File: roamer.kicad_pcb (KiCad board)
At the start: 2 copper layers, 0 parts

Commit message: Fixing footprint imports
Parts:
- added C1: 10uF, Inductor_SMD:L_0805_2012Metric, F.Cu at (194.5, 139.5)
- added C10: 10uF, Inductor_SMD:L_0805_2012Metric, F.Cu at (233.5, 128.4)
- added C11: 1uF, Capacitor_SMD:C_0603_1608Metric, F.Cu at (237.8, 122.5)
- added C12: 1uF, Capacitor_SMD:C_0603_1608Metric, F.Cu at (233.2, 100.8)
- added C13: 10uF, Inductor_SMD:L_0805_2012Metric, F.Cu at (226.7, 115.4)
- added C14: 1uF, Capacitor_SMD:C_0603_1608Metric, F.Cu at (226.8, 96.2)
- added C15: 1uF, Capacitor_SMD:C_0603_1608Metric, F.Cu at (226.8, 98.7)
- added C2: 22pF, Capacitor_SMD:C_0603_1608Metric, F.Cu at (198.7, 150.8)
- added C3: 10uF, Inductor_SMD:L_0805_2012Metric, F.Cu at (217.9, 150.5)
- added C4: 22pF, Capacitor_SMD:C_0603_1608Metric, F.Cu at (198.7, 153.3)
- added C5: 10uF, Inductor_SMD:L_0805_2012Metric, F.Cu at (233.5, 120.2)
- added C6: 10uF, Inductor_SMD:L_0805_2012Metric, F.Cu at (233.5, 122.9)
- added C7: 1uF, Capacitor_SMD:C_0603_1608Metric, F.Cu at (237.8, 120.0)
- added C8: 10uF, Inductor_SMD:L_0805_2012Metric, F.Cu at (233.5, 125.7)
- added C9: 10uF, Inductor_SMD:L_0805_2012Metric, F.Cu at (194.5, 113.9)
- added CHG1: ORANGE, LED_SMD:LED_0805_2012Metric, F.Cu at (222.4, 150.7)
- added D1: WS2812B3535, LED_SMD:LED_SK6812MINI_PLCC4_3.5x3.5mm_P1.75mm, F.Cu at (241.2, 151.1)
- added D4: MBR120, Diode_SMD:D_SOD-123, F.Cu at (242.9, 132.6)
- added J1: Conn_Coaxial_Small, Connector_Coaxial:U.FL_Molex_MCRF_73412-0110_Vertical, F.Cu at (189.2, 141.2)
- added J2: S2B-PH-K-SLFSN, footprints:CONN_S2B-PH-K-S_JST, F.Cu at (215.5, 142.1)
- added J3: Conn_02x05_Odd_Even, Connector_PinHeader_1.27mm:PinHeader_2x05_P1.27mm_Vertical_SMD, F.Cu at (236.0, 110.8)
- added J4: Conn_Coaxial_Small, Connector_Coaxial:U.FL_Molex_MCRF_73412-0110_Vertical, F.Cu at (189.2, 115.6)
- added J8: MEM2075-00-140-01-A, footprints:GCT_MEM2075-00-140-01-A, F.Cu at (219.4, 132.0)
- added JP1: SolderJumper_2_Open, Jumper:SolderJumper-2_P1.3mm_Open_TrianglePad1.0x1.5mm, F.Cu at (227.0, 106.7)
- added L1: RED, LED_SMD:LED_0805_2012Metric, F.Cu at (221.7, 114.5)
- added L2: 10uH, Inductor_SMD:L_1008_2520Metric, F.Cu at (222.0, 111.2)
- added MCU1: ATSAMD51J19A-A, Package_QFP:TQFP-64_10x10mm_P0.5mm, F.Cu at (217.6, 102.1)
- added Q3: DMP2070UQ-7, Package_TO_SOT_SMD:SOT-23-5_HandSoldering, F.Cu at (242.7, 121.2)
- added R1: 10K, Resistor_SMD:R_0603_1608Metric, F.Cu at (233.2, 103.3)
- added R2: 1K, Capacitor_SMD:C_0603_1608Metric, F.Cu at (222.2, 140.3)
- added R3: 10K, Resistor_SMD:R_0603_1608Metric, F.Cu at (237.8, 125.1)
- added R4: 10K, Resistor_SMD:R_0603_1608Metric, F.Cu at (222.2, 142.8)
- added R6: 10K, Resistor_SMD:R_0603_1608Metric, F.Cu at (226.8, 101.2)
- added R7: 2.2K, Resistor_SMD:R_0603_1608Metric, F.Cu at (226.8, 103.7)
- added R9A1: 100K, Resistor_SMD:R_Array_Convex_4x1206, F.Cu at (216.8, 112.7)
- added R9B1: 100K, Resistor_SMD:R_Array_Convex_4x0603, F.Cu at (226.5, 111.7)
- added R9C1: 100K, Resistor_SMD:R_Array_Convex_4x0603, F.Cu at (237.9, 128.7)
- added R9D1: 100K, Resistor_SMD:R_Array_Convex_4x1206, F.Cu at (242.6, 98.3)
- added SW1: KMR2, Button_Switch_SMD:SW_Push_1P1T_NO_CK_KMR2, F.Cu at (234.5, 97.3)
- added TP1: TestPoint, TestPoint:TestPoint_Pad_D1.5mm, F.Cu at (212.2, 111.1)
- added TP2: TestPoint, TestPoint:TestPoint_Pad_D1.5mm, F.Cu at (212.2, 114.6)
- added TP3: TestPoint, TestPoint:TestPoint_Pad_D1.0mm, F.Cu at (238.1, 140.5)
- added TP4: TestPoint, TestPoint:TestPoint_Pad_D1.0mm, F.Cu at (238.1, 143.6)
- added U1: 2MB Flash, Package_SO:SOIC-8_3.9x4.9mm_P1.27mm, F.Cu at (190.4, 149.6)
- added U2: AP2112K-3.3, Package_TO_SOT_SMD:SOT-23-5, F.Cu at (242.5, 128.7)
- added U3: MCP73831-2-OT, Package_TO_SOT_SMD:SOT-23-5, F.Cu at (213.0, 151.5)
- added U4: RFM95W-915S2, RF_Module:HOPERF_RFM9XW_SMD, F.Cu at (196.0, 129.4)
- added U5: RFM69W, RF_Module:HOPERF_RFM69HW, F.Cu at (197.3, 103.8)
- added U7: BME688, Package_LGA:Bosch_LGA-8_3x3mm_P0.8mm_ClockwisePinNumbering, F.Cu at (206.2, 148.7)
- added U8: INA260, Package_SO:TSSOP-16_4.4x5mm_P0.65mm, F.Cu at (231.4, 151.9)
- added X2: 32.768 kHz, Crystal:Crystal_SMD_3215-2Pin_3.2x1.5mm, F.Cu at (199.2, 147.9)
- added X3: microUSB 2.0 B, Connector_USB:USB_Micro-B_Amphenol_10118194_Horizontal, F.Cu at (231.6, 142.1)

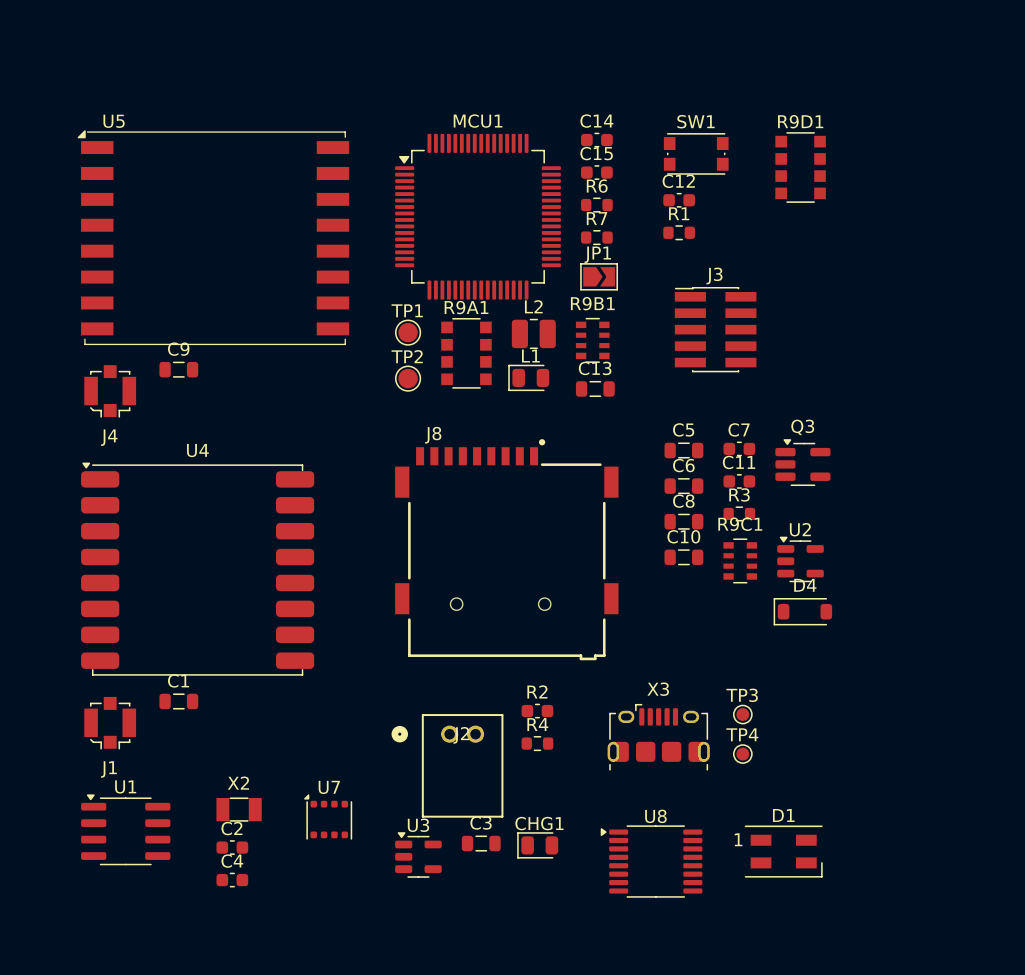
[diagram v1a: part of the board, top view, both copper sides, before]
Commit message: Spamming 0 ohm resistors
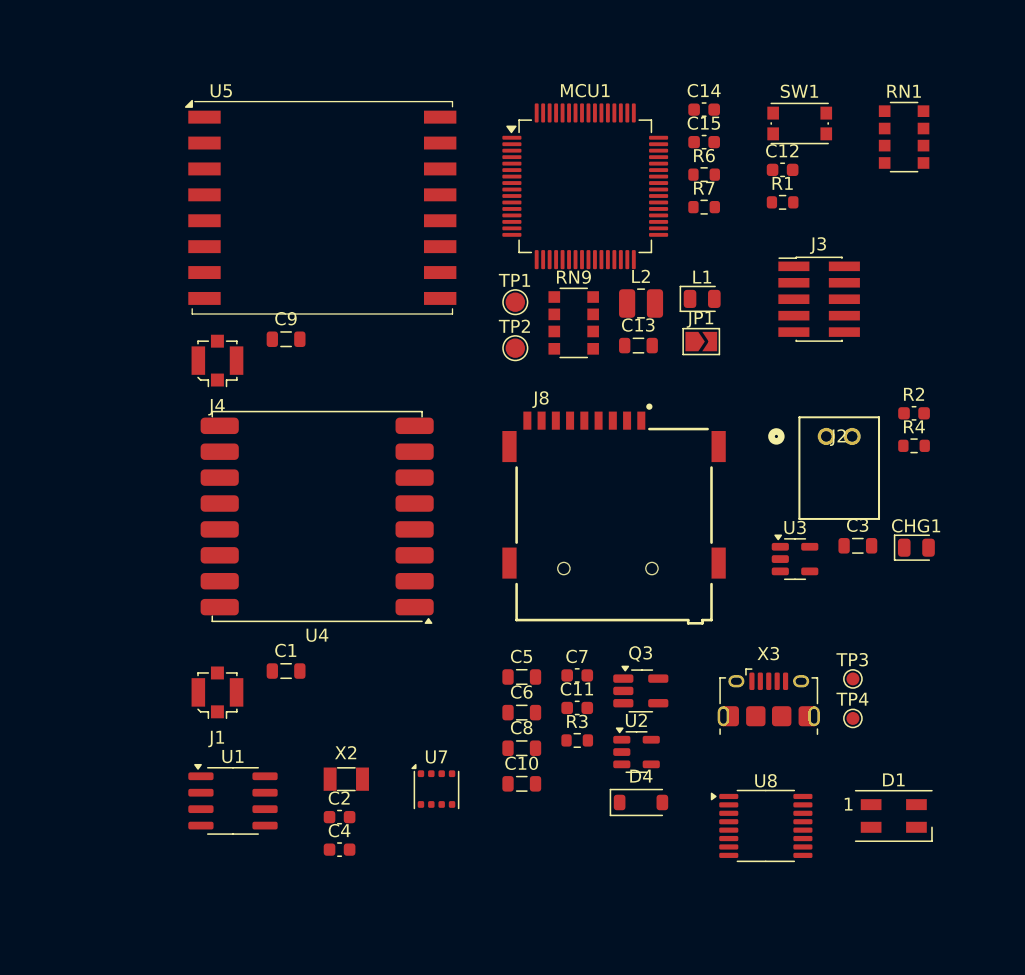
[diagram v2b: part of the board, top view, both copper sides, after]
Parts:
- removed R9A1, R9D1: 100K, Resistor_SMD:R_Array_Convex_4x1206
- removed R9B1, R9C1: 100K, Resistor_SMD:R_Array_Convex_4x0603
- added RN1: 100K, Resistor_SMD:R_Array_Convex_4x1206, F.Cu at (250.5, 96.0)
- added RN9: 100K, Resistor_SMD:R_Array_Convex_4x1206, F.Cu at (225.0, 110.3)
- moved CHG1 37.1 mm to (251.5, 127.7)
- moved U3 37.1 mm to (242.1, 128.5)
- moved J2 37.1 mm to (244.5, 119.1)
- moved R2 37.1 mm to (251.3, 117.3)
- moved C3 37.1 mm to (247.0, 127.5)
- moved R4 37.1 mm to (251.3, 119.8)
- moved Q3 21.5 mm to (230.2, 138.7)
- moved C10 21.5 mm to (221.0, 145.9)
- moved C5 21.5 mm to (221.0, 137.6)
- moved C6 21.5 mm to (221.0, 140.4)
- moved C7 21.5 mm to (225.3, 137.5)
- moved C8 21.5 mm to (221.0, 143.1)
- moved C11 21.5 mm to (225.3, 140.0)
- moved R3 21.5 mm to (225.3, 142.5)
- moved D4 19.4 mm to (230.2, 147.3)
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
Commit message: Starting layout
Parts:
- removed RN1, RN9: 100K, Resistor_SMD:R_Array_Convex_4x1206
- added D2: 1N4148, Diode_SMD:D_SOD-323F, F.Cu at (208.9, 230.5)
- added D3: 1N4148, Diode_SMD:D_SOD-323F, F.Cu at (208.9, 233.4)
- added JP2: SolderJumper_2_Open, Jumper:SolderJumper-2_P1.3mm_Open_TrianglePad1.0x1.5mm, F.Cu at (289.2, 135.2)
- added JP3: SolderJumper_2_Open, Jumper:SolderJumper-2_P1.3mm_Open_TrianglePad1.0x1.5mm, F.Cu at (230.3, 221.5)
- added R10: 0, Resistor_SMD:R_0603_1608Metric, F.Cu at (146.3, 82.2)
- added R11: 0, Resistor_SMD:R_0603_1608Metric, F.Cu at (146.3, 84.8)
- added R12: 0, Resistor_SMD:R_0603_1608Metric, F.Cu at (118.1, 79.7)
- added R13: 0, Resistor_SMD:R_0603_1608Metric, F.Cu at (118.1, 82.2)
- added R14: 0, Resistor_SMD:R_0603_1608Metric, F.Cu at (118.1, 84.8)
- added R15: 0, Resistor_SMD:R_0603_1608Metric, F.Cu at (118.1, 87.3)
- added R16: 0, Resistor_SMD:R_0603_1608Metric, F.Cu at (276.4, 149.3)
- added R17: 0, Resistor_SMD:R_0603_1608Metric, F.Cu at (276.4, 151.8)
- added R18: 0, Resistor_SMD:R_0603_1608Metric, F.Cu at (276.4, 154.4)
- added R19: 0, Resistor_SMD:R_0603_1608Metric, F.Cu at (276.4, 156.9)
- added R20: 10K, Resistor_SMD:R_0603_1608Metric, F.Cu at (146.3, 87.3)
- added R21: 0, Resistor_SMD:R_0603_1608Metric, F.Cu at (276.4, 159.4)
- added R22: 0, Resistor_SMD:R_0603_1608Metric, F.Cu at (146.3, 89.8)
- added R23: 10K, Resistor_SMD:R_0603_1608Metric, F.Cu at (194.3, 80.0)
- added R24: 0, Resistor_SMD:R_0603_1608Metric, F.Cu at (285.0, 130.0)
- added R25: 0, Resistor_SMD:R_0603_1608Metric, F.Cu at (285.0, 132.5)
- added R26: 0, Resistor_SMD:R_0603_1608Metric, F.Cu at (285.0, 135.0)
- added R27: 0, Resistor_SMD:R_0603_1608Metric, F.Cu at (200.1, 224.3)
- added R28: 0, Resistor_SMD:R_0603_1608Metric, F.Cu at (200.1, 226.8)
- added R29: 10K, Resistor_SMD:R_0603_1608Metric, F.Cu at (285.0, 137.5)
- added R30: 10K, Resistor_SMD:R_0603_1608Metric, F.Cu at (296.2, 149.3)
- added R31: 10K, Resistor_SMD:R_0603_1608Metric, F.Cu at (296.2, 151.8)
- added R32: 10K, Resistor_SMD:R_0603_1608Metric, F.Cu at (200.1, 229.3)
- added R33: 0, Resistor_SMD:R_0603_1608Metric, F.Cu at (146.3, 92.3)
- added R34: 10K, Resistor_SMD:R_0603_1608Metric, F.Cu at (194.3, 82.5)
- added R35: 0, Resistor_SMD:R_0603_1608Metric, F.Cu at (146.3, 94.8)
- added R36: 10K, Resistor_SMD:R_0603_1608Metric, F.Cu at (118.1, 89.8)
- added R37: 0, Resistor_SMD:R_0603_1608Metric, F.Cu at (146.3, 97.3)
- added R39: 0, Resistor_SMD:R_0603_1608Metric, F.Cu at (118.1, 92.3)
- added R41: 0, Resistor_SMD:R_0603_1608Metric, F.Cu at (200.1, 231.8)
- added R42: 0, Resistor_SMD:R_0603_1608Metric, F.Cu at (200.1, 234.3)
- added R43: 0, Resistor_SMD:R_0603_1608Metric, F.Cu at (200.1, 236.8)
- added R44: 10K, Resistor_SMD:R_0603_1608Metric, F.Cu at (118.1, 94.8)
- added R45: 0, Resistor_SMD:R_0603_1608Metric, F.Cu at (118.1, 97.3)
- added R5: 10K, Resistor_SMD:R_0603_1608Metric, F.Cu at (200.1, 221.8)
- added R8: 10K, Resistor_SMD:R_0603_1608Metric, F.Cu at (146.3, 79.7)
- added R9: 100K, Resistor_SMD:R_Array_Convex_4x1206, F.Cu at (212.2, 109.2)
- added TP10: TestPoint, TestPoint:TestPoint_Loop_D2.50mm_Drill1.0mm, F.Cu at (204.4, 231.3)
- added TP11: TestPoint, TestPoint:TestPoint_Loop_D2.50mm_Drill1.0mm, F.Cu at (204.4, 236.0)
- added TP12: TestPoint, TestPoint:TestPoint_Loop_D2.50mm_Drill1.0mm, F.Cu at (122.4, 98.4)
- added TP13: TestPoint, TestPoint:TestPoint_Loop_D2.50mm_Drill1.0mm, F.Cu at (122.4, 103.1)
- added TP14: TestPoint, TestPoint:TestPoint_Loop_D2.50mm_Drill1.0mm, F.Cu at (150.7, 98.4)
- added TP15: TestPoint, TestPoint:TestPoint_Loop_D2.50mm_Drill1.0mm, F.Cu at (150.7, 103.0)
- added TP16: TestPoint, TestPoint:TestPoint_Loop_D2.50mm_Drill1.0mm, F.Cu at (291.8, 155.1)
- added TP17: TestPoint, TestPoint:TestPoint_Loop_D2.50mm_Drill1.0mm, F.Cu at (191.7, 230.7)
- added TP18: TestPoint, TestPoint:TestPoint_Loop_D2.50mm_Drill1.0mm, F.Cu at (191.7, 235.3)
- added TP5: TestPoint, TestPoint:TestPoint_Loop_D2.50mm_Drill1.0mm, F.Cu at (191.7, 226.0)
- added TP6: TestPoint, TestPoint:TestPoint_Loop_D2.50mm_Drill1.0mm, F.Cu at (291.8, 150.4)
- added TP7: TestPoint, TestPoint:TestPoint_Loop_D2.50mm_Drill1.0mm, F.Cu at (220.8, 226.7)
- added TP8: TestPoint, TestPoint:TestPoint_Loop_D2.50mm_Drill1.0mm, F.Cu at (280.7, 157.0)
- added TP9: TestPoint, TestPoint:TestPoint_Loop_D2.50mm_Drill1.0mm, F.Cu at (280.7, 161.7)
- moved CHG1 126.4 mm to (185.2, 235.3)
- moved R2 126.4 mm to (185.0, 224.9)
- moved U3 126.4 mm to (175.8, 236.2)
- moved C3 126.4 mm to (180.7, 235.2)
- moved R4 126.4 mm to (185.0, 227.4)
- moved C12 122.5 mm to (236.5, 220.9)
- moved R1 122.5 mm to (236.5, 223.4)
- moved SW1 118.9 mm to (244.7, 213.8)
- moved L1 107.7 mm to (208.8, 213.0)
- moved C13 107.7 mm to (203.9, 216.6)
- moved JP1 107.7 mm to (208.8, 216.2)
- moved L2 107.7 mm to (204.1, 213.3)
- moved TP1 106.5 mm to (199.8, 213.2)
- moved TP2 106.5 mm to (199.8, 216.8)
- moved C2 87.9 mm to (236.5, 231.2)
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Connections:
- net +3.3V renamed Net-(U7-VDD)
- net /Power - Battery/STAT renamed Net-(U3-STAT)
- C1 pad 2: +3V3 -> Net-(U4-3.3V)
- C9 pad 2: +3V3 -> Net-(U5-3.3V)
- J3 pad 1: unconnected-(J3-Pin_1-Pad1) -> Net-(J3-Pin_1)
- J3 pad 10: /MCU/I2C.SDA -> Net-(D3-K)
- J3 pad 2: unconnected-(J3-Pin_2-Pad2) -> Net-(J3-Pin_1)
- J3 pad 3: unconnected-(J3-Pin_3-Pad3) -> GND
- J3 pad 4: unconnected-(J3-Pin_4-Pad4) -> GND
- J3 pad 5: unconnected-(J3-Pin_5-Pad5) -> Net-(D2-K)
- J3 pad 7: unconnected-(J3-Pin_7-Pad7) -> Net-(J3-Pin_7)
- J3 pad 8: /MCU/I2C.SCL -> unconnected-(J3-Pin_8-Pad8)
- J3 pad 9: unconnected-(J3-Pin_9-Pad9) -> Net-(J3-Pin_9)
- J8 pad P3: /Comms - LoRa 433/SPI.MOSI -> /Bus - SPI/SPI.MOSI
- J8 pad P5: /Comms - LoRa 433/SPI.SCK -> /Bus - SPI/SPI.SCK
- J8 pad P7: /Comms - LoRa 433/SPI.MISO -> /Bus - SPI/SPI.MISO
- J8 pad P9: /Interface - uSD/CARD_DETECT -> unconnected-(J8-CD-PadP9)
- MCU1 pad 11: /MCU/A2 -> unconnected-(MCU1-PB08-Pad11)
- MCU1 pad 12: /MCU/A3 -> unconnected-(MCU1-PB09-Pad12)
- MCU1 pad 26: /Comms - LoRa 900/CS_LORA_900 -> unconnected-(MCU1-PB13-Pad26)
- MCU1 pad 27: /Comms - LoRa 433/CS_LORA_433 -> unconnected-(MCU1-PB14-Pad27)
- MCU1 pad 28: /Interface - uSD/CS_uSD -> unconnected-(MCU1-PB15-Pad28)
- MCU1 pad 29: /MCU/I2C.SDA -> /Bus - I2C/I2C.SDA
- MCU1 pad 30: /MCU/I2C.SCL -> /Bus - I2C/I2C.SCL
- MCU1 pad 31: unconnected-(MCU1-PA14-Pad31) -> /Comms - LoRa 900/CS_LORA_900
- MCU1 pad 35: unconnected-(MCU1-PA16-Pad35) -> /Comms - LoRa 433/CS_LORA_433
- MCU1 pad 36: unconnected-(MCU1-PA17-Pad36) -> /Bus - SPI/SPI.SCK
- MCU1 pad 37: unconnected-(MCU1-PA18-Pad37) -> /Interface - uSD/CS_uSD
- MCU1 pad 38: unconnected-(MCU1-PA19-Pad38) -> /Comms - LoRa 900/~{RESET_LORA_900}
- MCU1 pad 39: /MCU/TX_D1 -> unconnected-(MCU1-PB16-Pad39)
- MCU1 pad 40: /MCU/RX_D0 -> unconnected-(MCU1-PB17-Pad40)
- MCU1 pad 41: unconnected-(MCU1-PA20-Pad41) -> /Comms - LoRa 433/~{RESET_LORA_433}
- MCU1 pad 42: unconnected-(MCU1-PA21-Pad42) -> /MCU/~{AIRQ_RESET}
- MCU1 pad 43: unconnected-(MCU1-PA22-Pad43) -> /MCU/AIRQ_SET
- MCU1 pad 49: /Comms - LoRa 433/SPI.MISO -> /Bus - SPI/SPI.MISO
- MCU1 pad 50: /Comms - LoRa 433/SPI.MOSI -> /Bus - SPI/SPI.MOSI
- MCU1 pad 59: /Comms - LoRa 900/~{RESET_LORA_900} -> unconnected-(MCU1-PB30-Pad59)
- MCU1 pad 60: /Comms - LoRa 433/~{RESET_LORA_433} -> unconnected-(MCU1-PB31-Pad60)
- MCU1 pad 7: unconnected-(MCU1-GNDANA-Pad7) -> GND
- U4 pad 13: +3V3 -> Net-(U4-3.3V)
- U4 pad 2: /Comms - LoRa 433/SPI.MISO -> Net-(U4-MISO)
- U4 pad 3: /Comms - LoRa 433/SPI.MOSI -> Net-(U4-MOSI)
- U4 pad 4: /Comms - LoRa 433/SPI.SCK -> Net-(U4-SCK)
- U4 pad 5: /Comms - LoRa 900/CS_LORA_900 -> Net-(U4-NSS)
- U4 pad 6: /Comms - LoRa 900/~{RESET_LORA_900} -> Net-(U4-RESET)
- U5 pad 1: /Comms - LoRa 433/~{RESET_LORA_433} -> Net-(U5-RESET)
- U5 pad 12: /Comms - LoRa 433/SPI.SCK -> Net-(U5-SCK)
- U5 pad 13: /Comms - LoRa 433/SPI.MOSI -> Net-(U5-MISO)
- U5 pad 14: /Comms - LoRa 433/SPI.MISO -> Net-(U5-MOSI)
- U5 pad 15: /Comms - LoRa 433/CS_LORA_433 -> Net-(U5-NSS)
- U5 pad 8: +3V3 -> Net-(U5-3.3V)
- U7 pad 2: /Sensor - Atmosphere/CS_3V -> unconnected-(U7-CSB-Pad2)
- U7 pad 3: /MCU/I2C.SDA -> Net-(U7-SDI)
- U7 pad 4: /MCU/I2C.SCL -> Net-(U7-SCK)
- U7 pad 5: /Sensor - Atmosphere/SDO/ADR -> Net-(JP2-B)
- U8 pad 1: +BATT -> Net-(U8-VBUS)
- U8 pad 10: unconnected-(U8-VS-Pad10) -> Net-(U8-VS)
- U8 pad 12: +BATT -> Net-(U8-VBUS)
- U8 pad 14: /Power - Management/IN- -> Net-(R21-Pad1)
- U8 pad 15: /Power - Management/IN- -> Net-(R21-Pad1)
- U8 pad 16: /Power - Management/IN- -> Net-(R21-Pad1)
- U8 pad 2: +BATT -> Net-(U8-VBUS)
- U8 pad 3: +BATT -> Net-(U8-VBUS)
- U8 pad 8: /MCU/I2C.SDA -> Net-(U8-SDA)
- U8 pad 9: /MCU/I2C.SCL -> Net-(U8-SCL)
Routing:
- net /MCU - Memory/QSPI.DATA0: track 0.00 -> 11.9 mm, vias 0 -> 2
- net /MCU - Memory/QSPI.SCK: track 0.00 -> 9.16 mm, vias 0 -> 2
- net /MCU - Memory/QSPI.CS: track 0.00 -> 8.95 mm, vias 0 -> 2
- net /MCU - Memory/QSPI.DATA2: track 0.00 -> 8.85 mm
- net /MCU - Memory/QSPI.DATA3: track 0.00 -> 7.81 mm
- net /MCU - Memory/QSPI.DATA1: track 0.00 -> 7.37 mm
- net +3V3: track 0.00 -> 5.91 mm, vias 0 -> 2
- net GND: track 0.00 -> 4.59 mm, vias 0 -> 2
